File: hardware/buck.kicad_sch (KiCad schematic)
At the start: 9 parts, among them U3 TP6841S6-A

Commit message: Finished first iteration of the PCB
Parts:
- renumbered C3 to C6, C4 to C7, C5 to C8, C6 to C9, R1 to R13, R2 to R14, R3 to R15, U3 to U5
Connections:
- net Vin renamed V_in
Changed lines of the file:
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@@
-    (stroke (width 0) (type default) (color 0 0 0 0))
-  )
-  (wire (pts (xy 121.92 54.61) (xy 133.35 54.61))
     (stroke (width 0) (type default) (color 0 0 0 0))
   )
@@
   )
   (wire (pts (xy 54.61 62.23) (xy 54.61 58.42))
+    (stroke (width 0) (type default) (color 0 0 0 0))
+  )
+  (wire (pts (xy 121.92 50.165) (xy 121.92 54.61))
     (stroke (width 0) (type default) (color 0 0 0 0))
   )
@@
     (effects (font (size 0.635 0.635)) (justify left bottom))
   )
-  (global_label "Vin" (shape input) (at 38.1 49.53 180) (fields_autoplaced)
+  (hierarchical_label "V_in" (shape input) (at 38.1 49.53 180)
     (effects (font (size 1.27 1.27)) (justify right))
-    (property "Intersheet References" "${INTERSHEET_REFS}" (id 0) (at 32.8445 49.4506 0)
-      (effects (font (size 1.27 1.27)) (justify right) hide)
-    )
   )
   (symbol (lib_id "power:GND") (at 85.09 77.47 0) (unit 1)
     (in_bom yes) (on_board yes) (fields_autoplaced)
-    (property "Reference" "#PWR011" (id 0) (at 85.09 83.82 0)
+    (property "Reference" "#PWR037" (id 0) (at 85.09 83.82 0)
       (effects (font (size 1.27 1.27)) hide)
     )
@@
     (pin "1")
   )
+  (symbol (lib_id "power:+5V") (at 121.92 50.165 0) (unit 1)
+    (in_bom yes) (on_board yes) (fields_autoplaced)
+    (property "Reference" "#PWR038" (id 0) (at 121.92 53.975 0)
+      (effects (font (size 1.27 1.27)) hide)
+    )
+    (property "Value" "+5V" (id 1) (at 121.92 46.5892 0))
+    (property "Footprint" "" (id 2) (at 121.92 50.165 0)
+      (effects (font (size 1.27 1.27)) hide)
+    )
+    (property "Datasheet" "" (id 3) (at 121.92 50.165 0)
+      (effects (font (size 1.27 1.27)) hide)
+    )
+    (pin "1")
+  )
   (symbol (lib_id "Device:R") (at 68.58 54.61 90) (unit 1)
     (in_bom yes) (on_board yes)
-    (property "Reference" "R1" (id 0) (at 68.58 57.15 90))
+    (property "Reference" "R13" (id 0) (at 68.58 57.15 90))
     (property "Value" "100k" (id 1) (at 68.58 52.4311 90))
     (property "Footprint" "Resistor_SMD:R_0402_1005Metric" (id 2) (at 68.58 56.388 90)
@@
     (pin "2")
   )
-  (symbol (lib_id "power:+5V") (at 133.35 54.61 270) (unit 1)
-    (in_bom yes) (on_board yes) (fields_autoplaced)
-    (property "Reference" "#PWR012" (id 0) (at 129.54 54.61 0)
-      (effects (font (size 1.27 1.27)) hide)
-    )
-    (property "Value" "+5V" (id 1) (at 136.525 55.0438 90)
-      (effects (font (size 1.27 1.27)) (justify left))
-    )
-    (property "Footprint" "" (id 2) (at 133.35 54.61 0)
-      (effects (font (size 1.27 1.27)) hide)
-    )
-    (property "Datasheet" "" (id 3) (at 133.35 54.61 0)
-      (effects (font (size 1.27 1.27)) hide)
-    )
-    (pin "1")
-  )
   (symbol (lib_id "Device:C_Small") (at 99.06 49.53 90) (unit 1)
     (in_bom yes) (on_board yes) (fields_autoplaced)
-    (property "Reference" "C5" (id 0) (at 99.0663 44.2681 90))
+    (property "Reference" "C8" (id 0) (at 99.0663 44.2681 90))
     (property "Value" "100n" (id 1) (at 99.0663 46.805 90))
     (property "Footprint" "Capacitor_SMD:C_0402_1005Metric" (id 2) (at 99.06 49.53 0)
@@
   (symbol (lib_id "custom:TP6841S6-A") (at 85.09 54.61 0) (unit 1)
     (in_bom yes) (on_board yes)
-    (property "Reference" "U3" (id 0) (at 85.09 43.18 0))
+    (property "Reference" "U5" (id 0) (at 85.09 43.18 0))
     (property "Value" "TP6841S6-A" (id 1) (at 85.09 45.72 0))
     (property "Footprint" "Package_TO_SOT_SMD:SOT-23-6" (id 2) (at 85.09 50.8 0)
@@
   (symbol (lib_id "Device:C_Small") (at 121.92 60.96 0) (unit 1)
     (in_bom yes) (on_board yes) (fields_autoplaced)
-    (property "Reference" "C6" (id 0) (at 124.2441 60.1316 0)
+    (property "Reference" "C9" (id 0) (at 124.2441 60.1316 0)
       (effects (font (size 1.27 1.27)) (justify left))
     )
@@
   (symbol (lib_id "Device:C_Small") (at 44.45 55.88 0) (unit 1)
     (in_bom yes) (on_board yes) (fields_autoplaced)
-    (property "Reference" "C3" (id 0) (at 46.7741 55.0516 0)
+    (property "Reference" "C6" (id 0) (at 46.7741 55.0516 0)
       (effects (font (size 1.27 1.27)) (justify left))
     )
@@
   (symbol (lib_id "power:GND") (at 49.53 66.04 0) (unit 1)
     (in_bom yes) (on_board yes) (fields_autoplaced)
-    (property "Reference" "#PWR010" (id 0) (at 49.53 72.39 0)
+    (property "Reference" "#PWR036" (id 0) (at 49.53 72.39 0)
       (effects (font (size 1.27 1.27)) hide)
     )
@@
   (symbol (lib_id "Device:C_Small") (at 54.61 55.88 180) (unit 1)
     (in_bom yes) (on_board yes) (fields_autoplaced)
-    (property "Reference" "C4" (id 0) (at 56.9341 55.0389 0)
+    (property "Reference" "C7" (id 0) (at 56.9341 55.0389 0)
       (effects (font (size 1.27 1.27)) (justify right))
     )
@@
   (symbol (lib_id "Device:R") (at 110.49 59.69 90) (unit 1)
     (in_bom yes) (on_board yes)
-    (property "Reference" "R3" (id 0) (at 110.49 62.23 90))
+    (property "Reference" "R15" (id 0) (at 110.49 62.23 90))
     (property "Value" "120k" (id 1) (at 110.49 57.5111 90))
     (property "Footprint" "Resistor_SMD:R_0402_1005Metric" (id 2) (at 110.49 61.468 90)
@@
   (symbol (lib_id "Device:R") (at 104.14 67.31 0) (unit 1)
     (in_bom yes) (on_board yes) (fields_autoplaced)
-    (property "Reference" "R2" (id 0) (at 105.918 66.4753 0)
-      (effects (font (size 1.27 1.27)) (justify left))
-    )
+    (property "Reference" "R14" (id 0) (at 105.918 66.4753 0)
+      (effects (font (size 1.27 1.27)) (justify left))
+    )

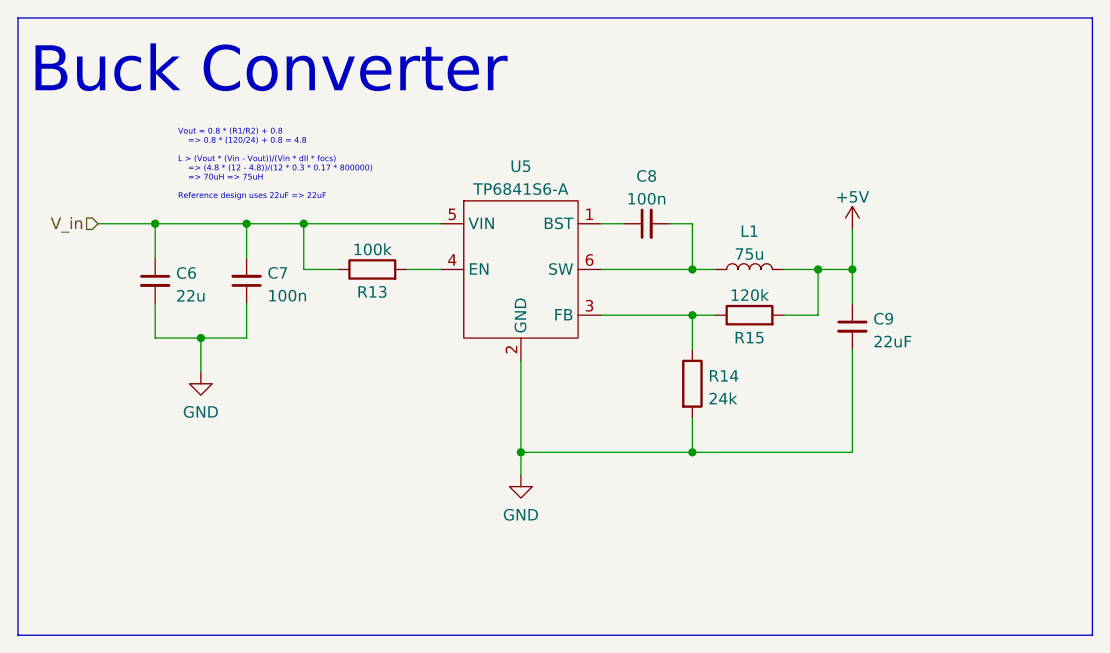
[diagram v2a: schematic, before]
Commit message: Updated to new version of KiCad and made some small changes to the design
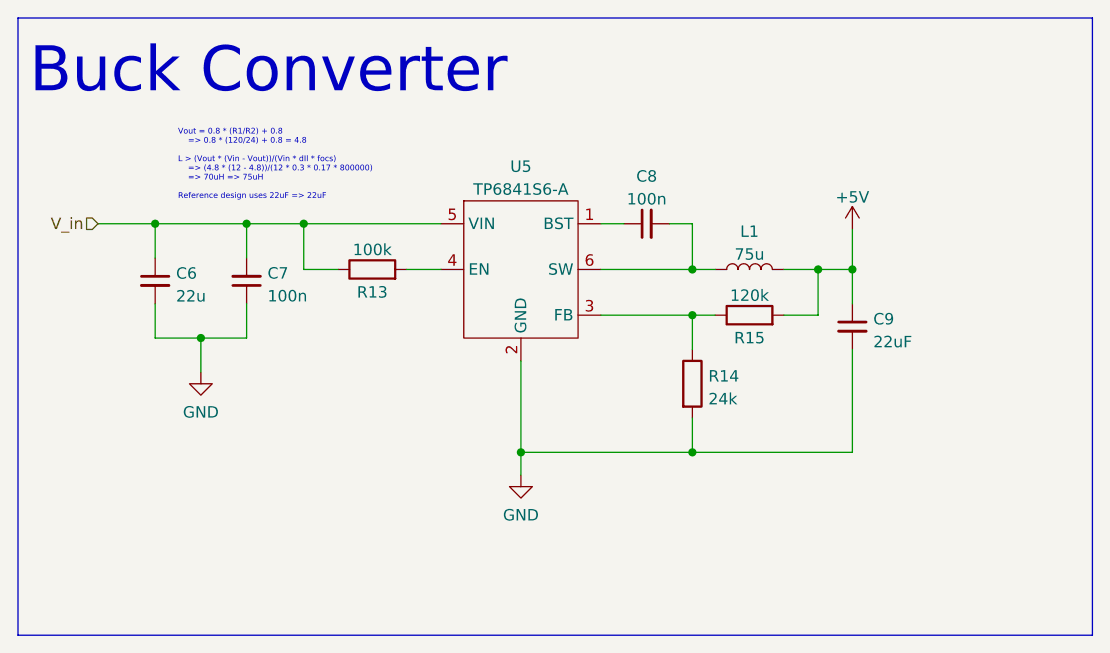
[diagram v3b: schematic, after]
